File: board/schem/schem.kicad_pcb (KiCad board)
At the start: 2 copper layers, 133 x 85 mm, 136 parts, among them J1 no_break, J10 no_hal, J11 break2, J12 impulse, J13 hal, J14 no_temp, J15 speed, J16 analog, J17 motor_tmp, J18 adc_red1, J19 adc_red2, J2 motor_out, J20 ON/OFF, J21 lamp, J3 test, J8 POWER_IN, J9 break1, Q1 BC817, Q2 BC807, Q3 BC817, Q4 BC817, Q5 BC807, Q6 BC817, Q7 BC817, Q8 BC807, Q9 BC817, SW1 SW_Push, SW2 SW_Push, T1 NTD5865NL, T2 FDD9507L, T3 NTD5865NL, T4 FDD9507L, T5 NTD5865NL, T6 FDD9507L, U1 CFPS-39-12M, U10 AP2138, U11 LD1117, U2 EP4CE6, U3 JTAG, U4 IFX27001TFV50, U5 LF33CDT, U6 IS25LQ, U7 MPC3008, U8 IFX27001TFV50, U9 IS25LQ

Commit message: some  progress in  board  development
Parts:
- added R37: 4.7k, Resistor_SMD:R_1206_3216Metric, F.Cu at (203.2, 55.7)
- R42: moved to B.Cu
- moved R43 23.5 mm to (179.8, 68.0), turned to 270 degrees
- moved R36 14.4 mm to (210.0, 63.2), turned to 180 degrees
- moved R42 13.7 mm to (198.8, 83.5)
- moved R35 12.6 mm to (203.4, 67.8), turned to 90 degrees
- moved C4 11.2 mm to (197.6, 55.8), turned to 180 degrees
- moved R34 5.30 mm to (210.1, 60.2), turned to 180 degrees
- moved R39 4.90 mm to (197.2, 67.9), turned to 270 degrees
- moved J2 2.38 mm to (159.0, 88.6)
- moved U6 1.88 mm to (201.3, 60.9), turned to 0 degrees
- moved F2 1.20 mm to (112.7, 86.7)
- moved C15 0.95 mm to (154.0, 130.9)
- moved SW2 0.35 mm to (197.7, 130.2)
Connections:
- J3 pad 3: /control/A4 -> /control/A3
- J3 pad 4: /control/A3 -> /control/A4
- R35 pad 1: /control/ASDO -> Net-(R35-Pad1)
- U2 pad 43: Net-(U2-Pad43) -> /DriveAndSens/A_p
- U2 pad 44: Net-(U2-Pad44) -> /DriveAndSens/A_n
- U2 pad 50: Net-(U2-Pad50) -> /DriveAndSens/B_p
- U2 pad 51: Net-(U2-Pad51) -> /DriveAndSens/B_n
- U2 pad 54: /DriveAndSens/A_p -> Net-(U2-Pad54)
- U2 pad 55: /DriveAndSens/A_n -> Net-(U2-Pad55)
- U2 pad 58: /DriveAndSens/B_p -> Net-(U2-Pad58)
- U2 pad 59: /DriveAndSens/B_n -> Net-(U2-Pad59)
- U2 pad 69: /control/D_break -> Net-(U2-Pad69)
- U2 pad 70: /control/D_tmp -> Net-(U2-Pad70)
- U2 pad 71: /control/D_diag -> Net-(U2-Pad71)
- U6 pad 1: /control/nCSO -> /control/nCEO
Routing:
- net GND: track 0.00 -> 789.8 mm, vias 0 -> 20
- net +3V3: track 0.00 -> 609.1 mm, vias 0 -> 16
- net +1V2: track 0.00 -> 222.0 mm, vias 0 -> 5
- net +36V: track 0.00 -> 202.1 mm, vias 0 -> 1
- net +5V: track 0.00 -> 161.8 mm, vias 0 -> 4
- net +2V5: track 0.00 -> 140.1 mm, vias 0 -> 4
- net /DriveAndSens/A_n: track 0.00 -> 122.7 mm, vias 0 -> 1
- net /DriveAndSens/C_out: track 0.00 -> 50.9 mm
- net /DriveAndSens/B_out: track 0.00 -> 49.0 mm
- net /DriveAndSens/A_p: track 0.00 -> 48.1 mm, vias 0 -> 1
- net /control/nCONFIG: track 0.00 -> 44.2 mm, vias 0 -> 2
- net /control/hal_A: track 0.00 -> 44.2 mm, vias 0 -> 1
- net /control/TCK: track 0.00 -> 42.6 mm, vias 0 -> 1
- net /DriveAndSens/A_out: track 0.00 -> 41.9 mm, vias 0 -> 1
- net /control/A2: track 0.00 -> 38.4 mm
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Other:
- board size 133 x 85 mm -> 133 x 86 mm
- net class Default: clearance 0.25 -> 0.2; trace_width 0.25 -> 0.2
- rule trace_clearance: 0.25 -> 0.2

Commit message: some  work  on pcb
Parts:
- J2: footprint Connector_Phoenix_MSTB:PhoenixContact_MSTBA_2,5_3-G-5,08_1x03_P5.08mm_Horizontal -> Connector_Phoenix_MSTB:PhoenixContact_MSTBVA_2,5_3-G-5,08_1x03_P5.08mm_Vertical
- J20, J8: footprint Connector_Phoenix_MSTB:PhoenixContact_MSTBA_2,5_2-G-5,08_1x02_P5.08mm_Horizontal -> Connector_Phoenix_MSTB:PhoenixContact_MSTBVA_2,5_2-G-5,08_1x02_P5.08mm_Vertical
- moved R8 8.44 mm to (129.3, 126.7)
- moved R40 2.92 mm to (190.2, 124.5)
- moved J20 2.60 mm to (107.7, 61.0)
- moved J8 2.55 mm to (107.7, 75.2)
- moved T2 2.23 mm to (145.8, 124.3)
- moved R7 1.16 mm to (141.8, 129.2)
- moved T4 0.60 mm to (134.9, 93.2)
- moved C13 0.21 mm to (191.4, 104.0)
- turned SW2 to 180 degrees
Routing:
- net /DriveAndSens/A_p: track 48.1 -> 179.6 mm
- net +36V: track 202.1 -> 328.5 mm, vias 1 -> 6
- net /DriveAndSens/B_p: track 8.85 -> 101.5 mm
- net /DriveAndSens/B_n: track 14.6 -> 102.8 mm
- net +3V3: track 609.1 -> 686.8 mm
- net /DriveAndSens/A_n: track 122.7 -> 193.5 mm
- net /DriveAndSens/A_out: track 41.9 -> 106.2 mm
- net +2V5: track 140.1 -> 185.8 mm, vias 4 -> 6
- net /DriveAndSens/C_p: track 13.2 -> 44.3 mm, vias 1 -> 3
- net /DriveAndSens/B_out: track 49.0 -> 70.7 mm
- net /DriveAndSens/C_n: track 26.4 -> 46.8 mm, vias 0 -> 3
- net GND: track 789.8 -> 807.9 mm, vias 20 -> 21
- net Net-(C18-Pad1): track 1.31 -> 18.9 mm
- net Net-(Q9-Pad3): track 16.3 -> 31.8 mm
- net Net-(F2-Pad1): track 20.3 -> 35.7 mm, vias 2 -> 0
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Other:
- net class energy: clearance 1 -> 0.2
- net class energy_mid: clearance 0.5 -> 0.2

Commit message: some  work  on  pcb
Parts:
- removed F3: 3A, Fuse:Fuse_2512_6332Metric
- added R49: 4.7k, Resistor_SMD:R_1206_3216Metric, F.Cu at (215.0, 70.6)
- added R50: 4.7k, Resistor_SMD:R_1206_3216Metric, F.Cu at (214.8, 73.8)
- added R51: 4.7k, Resistor_SMD:R_1206_3216Metric, F.Cu at (212.3, 58.8)
- added R52: 4.7k, Resistor_SMD:R_1206_3216Metric, F.Cu at (229.9, 67.8)
- added R53: 4.7k, Resistor_SMD:R_1206_3216Metric, F.Cu at (223.3, 74.9)
- added R54: 4.7k, Resistor_SMD:R_1206_3216Metric, F.Cu at (229.9, 70.6)
- added R55: 63.4k, Resistor_SMD:R_1206_3216Metric, F.Cu at (132.6, 110.0)
- added R56: 10.5k, Resistor_SMD:R_1206_3216Metric, F.Cu at (119.5, 108.1)
- added R57: 2k, Resistor_SMD:R_1206_3216Metric, F.Cu at (125.8, 105.2)
- added U12: 68u, Inductor_SMD:L_12x12mm_H4.5mm, F.Cu at (110.8, 91.5)
- C10: value 0.1u -> 0.01u
- C11: value 10u -> 220u
- C17: value 0.1u -> 220u; footprint Capacitor_SMD:C_1206_3216Metric -> Capacitor_THT:CP_Radial_D8.0mm_P3.50mm
- C18: value 10u -> 0.22u; footprint Capacitor_THT:CP_Radial_D8.0mm_P3.50mm -> Capacitor_SMD:C_1206_3216Metric
- C4, C5: moved to B.Cu
- U4: value IFX27001TFV50 -> IS25LQ; footprint Package_TO_SOT_SMD:TO-252-2 -> Package_SO:SOIC-8_3.9x4.9mm_P1.27mm
- U8: value IFX27001TFV50 -> A8498; footprint Package_TO_SOT_SMD:TO-252-2 -> Package_SO:SOIC-8_3.9x4.9mm_P1.27mm
- U9: value IS25LQ -> B350B; footprint Package_SO:SOIC-8_3.9x4.9mm_P1.27mm -> Diode_SMD:D_SMB
- moved U4 107.9 mm to (222.4, 70.0), turned to 0 degrees
- moved U9 101.6 mm to (125.6, 100.8), turned to 0 degrees
- moved C18 55.1 mm to (129.8, 116.7)
- moved C17 49.7 mm to (115.5, 103.7)
- moved U8 47.6 mm to (125.8, 110.4)
- moved C1 45.1 mm to (185.1, 67.9), turned to 180 degrees
- moved U1 38.8 mm to (185.1, 71.8), turned to 270 degrees
- moved C11 17.3 mm to (116.0, 113.5), turned to 180 degrees
- moved R34 12.2 mm to (198.2, 57.5), turned to 0 degrees
- moved C10 11.8 mm to (126.6, 116.8), turned to 90 degrees
- moved R43 9.68 mm to (188.8, 71.7), turned to 90 degrees
- moved C4 8.47 mm to (204.7, 60.3), turned to 270 degrees
- moved R39 7.38 mm to (198.3, 60.6), turned to 0 degrees
- moved F1 6.39 mm to (112.7, 66.5)
- moved C5 6.19 mm to (222.2, 70.1), turned to 270 degrees
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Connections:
- net /control/ch2 renamed Net-(U7-Pad6)
- net /control/ch3 renamed Net-(U7-Pad7)
- net /control/ch4 renamed Net-(U7-Pad8)
- C10 pad 2: GND -> Net-(C10-Pad2)
- C11 pad 1: +5V -> +36V
- C17 pad 1: +36V -> Net-(C17-Pad1)
- C18 pad 1: Net-(C18-Pad1) -> +36V
- D5 pad 1: Net-(D5-Pad1) -> /control/D_hal
- F2 pad 1: Net-(F2-Pad1) -> +5V
- F2 pad 2: +36V -> Net-(C17-Pad1)
- J21 pad 2: Net-(C18-Pad1) -> +5V
- R34 pad 1: +3V3 -> /control/DATA0
- R35 pad 2: Net-(R35-Pad2) -> /control/ASDO
- R39 pad 1: Net-(R39-Pad1) -> +3V3
- R39 pad 2: /control/DATA0 -> Net-(R39-Pad2)
- R41 pad 2: Net-(R41-Pad2) -> /control/nCE_1
- U1 pad 3: Net-(U1-Pad3) -> /control/CLKIN
- U2 pad 12: Net-(U2-Pad12) -> /control/SCK
- U2 pad 128: /control/nCE_1 -> /control/SO_1
- U2 pad 129: /control/SI_1 -> /control/SCK_1
- U2 pad 132: /control/SO_1 -> /control/nCE_1
- U2 pad 133: /control/SCK_1 -> /control/SI_1
- U2 pad 32: Net-(U2-Pad32) -> /control/hal_C
- U2 pad 60: /DriveAndSens/C_p -> Net-(U2-Pad60)
- U2 pad 64: /DriveAndSens/C_n -> Net-(U2-Pad64)
- U2 pad 67: Net-(U2-Pad67) -> /control/D_hal
- U2 pad 68: /control/D_hal -> /control/D_break
- U2 pad 69: Net-(U2-Pad69) -> /control/D_tmp
- U2 pad 70: Net-(U2-Pad70) -> /control/D_diag
- U2 pad 71: Net-(U2-Pad71) -> /DriveAndSens/C_p
- U2 pad 72: Net-(U2-Pad72) -> /DriveAndSens/C_n
- U4 pad 1: GND -> /control/nCE_1
- U4 pad 2: +5V -> Net-(R49-Pad2)
- U4 pad 3: Net-(F2-Pad1) -> Net-(R50-Pad2)
- U6 pad 2: Net-(R39-Pad1) -> Net-(R34-Pad2)
- U6 pad 3: Net-(R34-Pad2) -> Net-(R39-Pad2)
- U6 pad 5: Net-(R35-Pad2) -> Net-(R35-Pad1)
- U6 pad 7: Net-(R34-Pad2) -> Net-(R51-Pad1)
- U8 pad 1: GND -> Net-(C10-Pad2)
- U8 pad 2: Net-(C18-Pad1) -> GND
- U9 pad 1: /control/nCE_1 -> Net-(C17-Pad1)
- U9 pad 2: /control/SO_1 -> GND
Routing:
- net GND: track 807.9 -> 880.8 mm, vias 21 -> 24
- net /control/hal_C: track 0.00 -> 70.5 mm, vias 0 -> 1
- net /control/D_hal: track 0.00 -> 68.2 mm
- net /control/D_break: track 0.00 -> 63.2 mm
- net /control/D_tmp: track 0.00 -> 59.0 mm
- net /control/D_diag: track 0.00 -> 53.3 mm
- net Net-(C17-Pad1): track 0.00 -> 50.7 mm
- net Net-(F2-Pad1): track 35.7 -> 0.00 mm
- net /control/SCK: track 5.47 -> 40.8 mm
- net Net-(U12-Pad1): track 0.00 -> 29.5 mm
- net +36V: track 328.5 -> 300.8 mm
- net +3V3: track 686.8 -> 711.6 mm, vias 16 -> 18
- net Net-(R41-Pad2): track 22.2 -> 0.00 mm
- net Net-(C18-Pad1): track 18.9 -> 0.00 mm
- net /control/ASDO: track 0.00 -> 14.4 mm
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
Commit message: work  on  pcb
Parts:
- D1, D12, D13, D2, D3, D4: value D -> BYC10
- R16: value 10k -> 1k
- R17, R18, R19: value 10k -> 4.7k
- moved D4 46.0 mm to (150.2, 69.5), turned to 0 degrees
- moved D2 41.9 mm to (132.5, 111.2), turned to 0 degrees
- moved D3 23.8 mm to (149.4, 86.0), turned to 270 degrees
- moved D1 11.0 mm to (147.2, 104.5)
- moved D12 5.05 mm to (162.3, 105.0), turned to 180 degrees
- moved C10 2.02 mm to (125.8, 114.9), turned to 0 degrees
- moved D13 1.10 mm to (168.5, 124.1), turned to 180 degrees
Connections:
- C10 pad 1: +36V -> Net-(C10-Pad1)
- D1 pad 1: +36V -> (no net)
- D1 pad 2: /DriveAndSens/B_out -> +36V
- D1 pad 3: (no net) -> /DriveAndSens/A_out
- D12 pad 1: +36V -> (no net)
- D12 pad 2: /DriveAndSens/C_out -> +36V
- D12 pad 3: (no net) -> /DriveAndSens/C_out
- D13 pad 1: /DriveAndSens/C_out -> (no net)
- D13 pad 2: Net-(D13-Pad2) -> /DriveAndSens/C_out
- D13 pad 3: (no net) -> Net-(D13-Pad3)
- D2 pad 1: /DriveAndSens/B_out -> (no net)
- D2 pad 2: Net-(D2-Pad2) -> /DriveAndSens/A_out
- D2 pad 3: (no net) -> Net-(D2-Pad3)
- D3 pad 1: +36V -> (no net)
- D3 pad 2: /DriveAndSens/A_out -> +36V
- D3 pad 3: (no net) -> /DriveAndSens/B_out
- D4 pad 1: /DriveAndSens/A_out -> (no net)
- D4 pad 2: Net-(D4-Pad2) -> /DriveAndSens/B_out
- D4 pad 3: (no net) -> Net-(D4-Pad3)
- T1 pad 3: Net-(D4-Pad2) -> Net-(D2-Pad3)
- T3 pad 3: Net-(D2-Pad2) -> Net-(D4-Pad3)
- T5 pad 3: Net-(D13-Pad2) -> Net-(D13-Pad3)
- U12 pad 1: Net-(U12-Pad1) -> Net-(C10-Pad1)
- U2 pad 94: +3V3 -> +2V5
- U2 pad 96: +3V3 -> +2V5
- U8 pad 7: Net-(U12-Pad1) -> Net-(C10-Pad1)
- U9 pad 1: Net-(C17-Pad1) -> Net-(C10-Pad1)
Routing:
- net Net-(C10-Pad1): track 0.00 -> 33.4 mm
- net Net-(D2-Pad3): track 0.00 -> 30.3 mm
- net Net-(U12-Pad1): track 29.5 -> 0.00 mm
- net +2V5: track 185.8 -> 208.5 mm
- net Net-(D13-Pad2): track 13.4 -> 0.00 mm
- net Net-(D2-Pad2): track 13.0 -> 0.00 mm
- net /DriveAndSens/A_out: track 106.2 -> 94.0 mm
- net Net-(D4-Pad2): track 12.1 -> 0.00 mm
- net Net-(D4-Pad3): track 0.00 -> 10.9 mm
- net Net-(C17-Pad1): track 50.7 -> 40.5 mm
- net /DriveAndSens/B_out: track 70.7 -> 80.1 mm
- net /DriveAndSens/C_out: track 64.5 -> 70.9 mm
- net +3V3: track 711.6 -> 705.6 mm
- net Net-(D13-Pad3): track 0.00 -> 5.66 mm
- net +1V2: track 229.7 -> 233.5 mm
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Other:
- net class power_micro added: clearance 0.2, trace_width 0.4, via_dia 0.8, via_drill 0.4

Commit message: recent  changes
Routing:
- net +36V: track 302.0 -> 337.2 mm
- net +1V2: track 233.5 -> 245.8 mm
- added copper zone on B.Cu, net GND
- added copper zone on F.Cu, net GND
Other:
- board size 133 x 86 mm -> 133 x 87 mm
- net class energy_mid: trace_width 2 -> 3

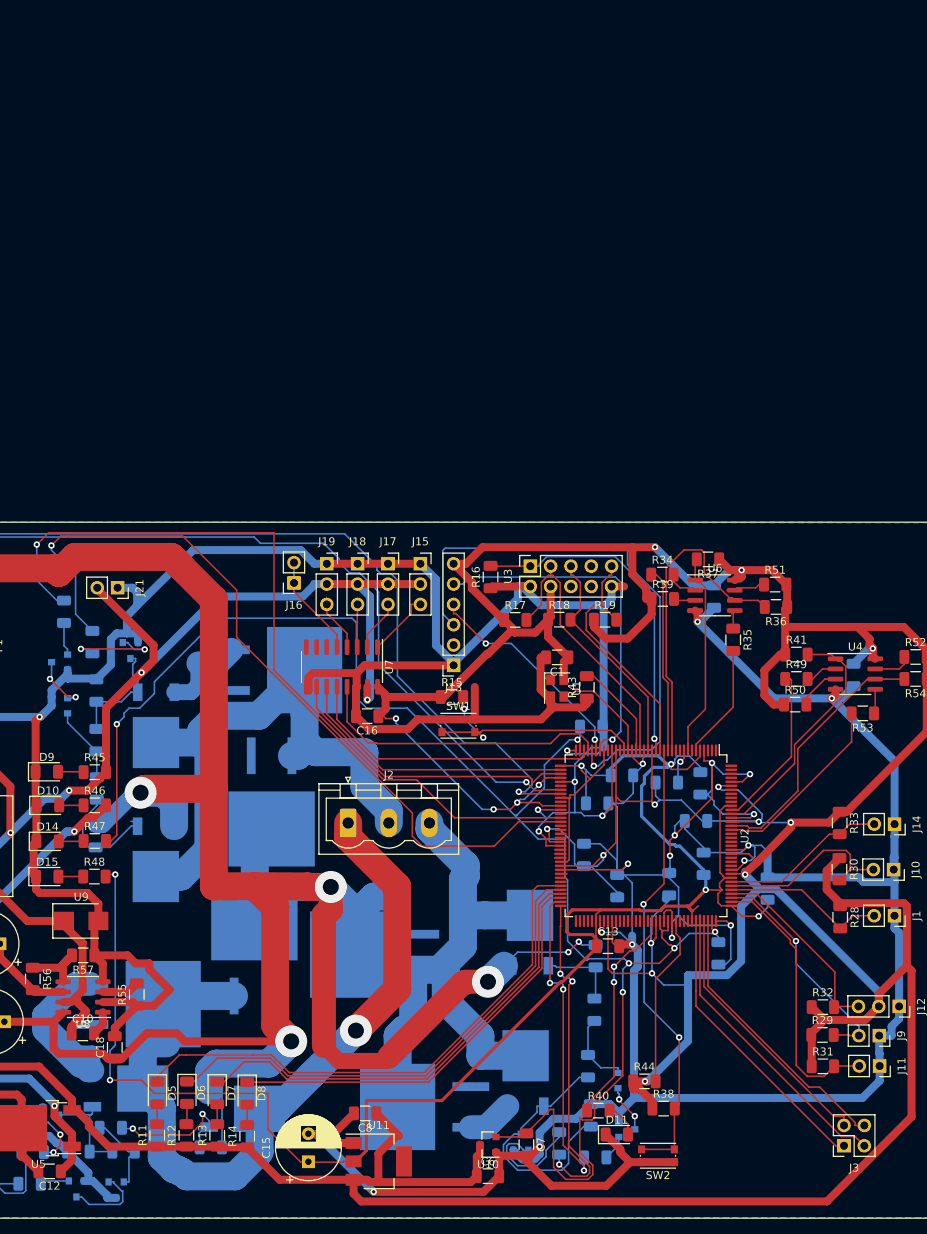
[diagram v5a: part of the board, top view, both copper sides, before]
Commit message: some  work  on schematic and  minor stuff in  adc  channel choice functionality
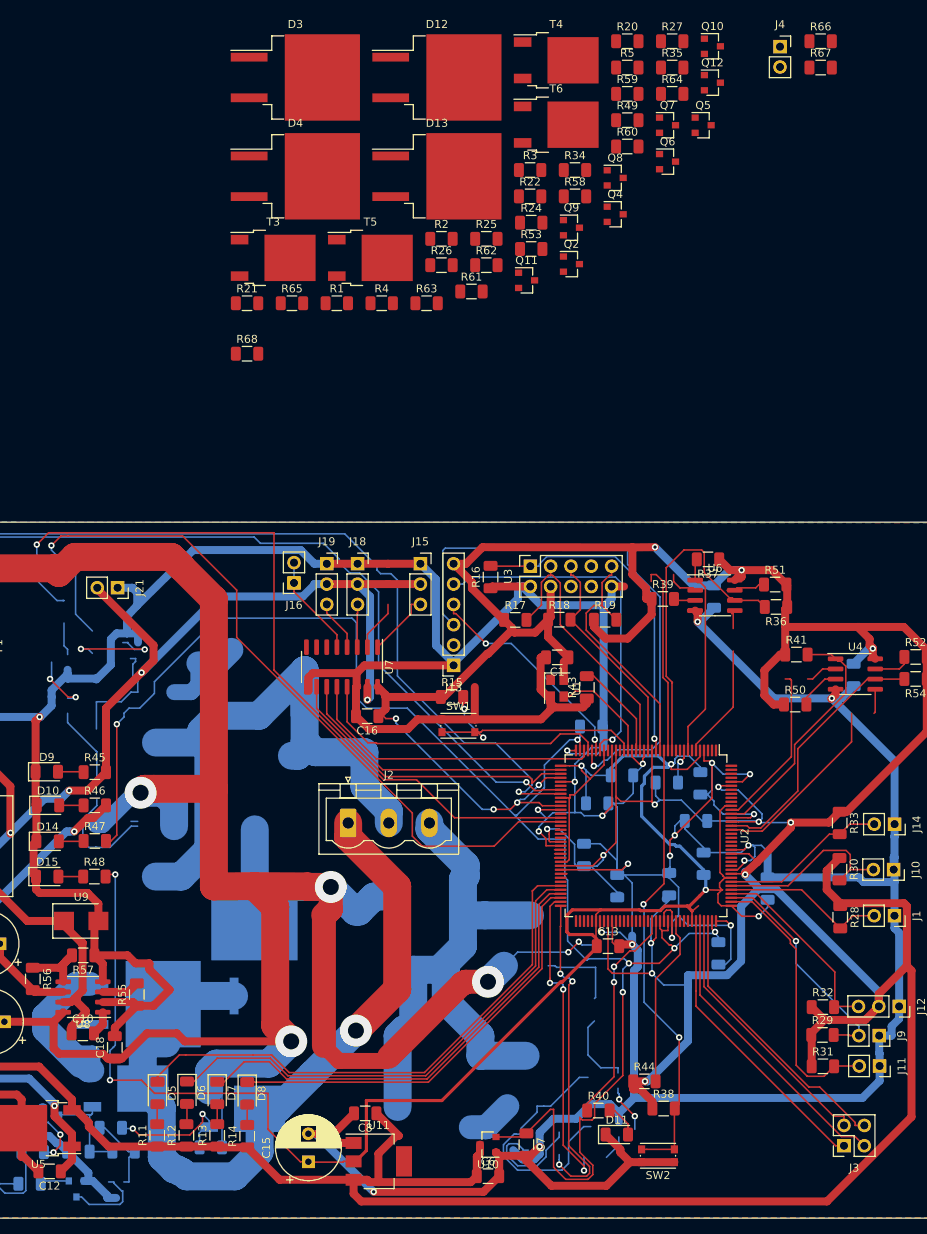
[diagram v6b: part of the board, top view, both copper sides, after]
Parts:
- removed J17: motor_tmp, Connector_PinSocket_2.54mm:PinSocket_1x03_P2.54mm_Vertical
- added J4: motor_tmp, Connector_PinSocket_2.54mm:PinSocket_1x02_P2.54mm_Vertical, F.Cu at (213.0, -8.43)
- added Q10: BC817, Package_TO_SOT_SMD:SOT-23, F.Cu at (204.5, -8.48)
- added Q11: BC817, Package_TO_SOT_SMD:SOT-23, F.Cu at (181.3, 20.8)
- added Q12: BC817, Package_TO_SOT_SMD:SOT-23, F.Cu at (204.5, -3.93)
- added R58: 8k, Resistor_SMD:R_1206_3216Metric, F.Cu at (187.3, 10.3)
- added R59: 100k, Resistor_SMD:R_1206_3216Metric, F.Cu at (193.9, -2.53)
- added R60: 10k, Resistor_SMD:R_1206_3216Metric, F.Cu at (193.9, 4.05)
- added R61: 4k, Resistor_SMD:R_1206_3216Metric, F.Cu at (174.4, 22.2)
- added R62: 10k, Resistor_SMD:R_1206_3216Metric, F.Cu at (176.2, 18.9)
- added R63: 10k, Resistor_SMD:R_1206_3216Metric, F.Cu at (168.8, 23.6)
- added R64: 10k, Resistor_SMD:R_1206_3216Metric, F.Cu at (199.5, -2.53)
- added R65: 10k, Resistor_SMD:R_1206_3216Metric, F.Cu at (151.9, 23.6)
- added R66: 4.7k, Resistor_SMD:R_1206_3216Metric, F.Cu at (218.0, -9.11)
- added R67: 4.7k, Resistor_SMD:R_1206_3216Metric, F.Cu at (218.0, -5.82)
- added R68: 120, Resistor_SMD:R_1206_3216Metric, F.Cu at (146.3, 29.9)
- D12, D13, D3, D4, Q4, Q6, Q7, Q9, R21, R22, T3, T4, T5, T6: moved to F.Cu
- Q2, Q5, Q8: value BC807 -> BC817; moved to F.Cu
- R1, R2: value 100k -> 2k; moved to F.Cu
- R10: value 7.5k -> 4k
- R20: value 7.5k -> 8k; moved to F.Cu
- R24: value 650 -> 10k; moved to F.Cu
- R25: value 2.2k -> 4k; moved to F.Cu
- R26: value 22k -> 2k; moved to F.Cu
- R27: value 7.5k -> 400k; moved to F.Cu
- R3: value 650 -> 400k; moved to F.Cu
- R34: value 4.7k -> 100k
- R35, R49: value 4.7k -> 10k
- R4: value 2.2k -> 100k; moved to F.Cu
- R5: value 22k -> 3k; moved to F.Cu
- R53: value 4.7k -> 3k
- R6: value 100k -> 400k
- R7: value 650 -> 3k
- R8: value 2.2k -> 8k
- R9: value 22k -> 10k
- moved R27 134.6 mm to (199.5, -9.11), turned to 0 degrees
- moved Q2 129.0 mm to (186.9, 18.7), turned to 0 degrees
- moved Q7 125.6 mm to (198.9, 1.39)
- moved R22 118.4 mm to (181.7, 10.3), turned to 0 degrees
- moved D13 116.3 mm to (170.1, 7.77), turned to 0 degrees
- moved R21 115.3 mm to (146.3, 23.6)
- moved Q9 114.5 mm to (186.9, 14.2), turned to 0 degrees
- moved Q8 112.8 mm to (192.4, 7.97)
- moved T4 111.8 mm to (185.0, -6.73), turned to 0 degrees
- moved D12 109.9 mm to (170.1, -4.58), turned to 0 degrees
- moved Q5 108.3 mm to (203.3, 1.39), turned to 0 degrees
- moved R5 107.1 mm to (193.9, -5.82), turned to 0 degrees
- moved R20 104.8 mm to (193.9, -9.11), turned to 0 degrees
- moved T5 103.7 mm to (161.8, 18.0), turned to 0 degrees
- moved R26 101.8 mm to (170.6, 18.9), turned to 0 degrees
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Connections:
- D11 pad 1: GND -> Net-(D11-Pad1)
- D11 pad 2: Net-(D11-Pad2) -> +3V3
- D13 pad 3: Net-(D13-Pad3) -> GND
- D2 pad 3: Net-(D2-Pad3) -> GND
- D4 pad 3: Net-(D4-Pad3) -> GND
- Q2 pad 1: Net-(Q1-Pad3) -> Net-(Q2-Pad1)
- Q2 pad 2: Net-(Q2-Pad2) -> GND
- Q2 pad 3: GND -> Net-(Q2-Pad3)
- Q4 pad 3: Net-(Q4-Pad3) -> Net-(Q3-Pad1)
- Q5 pad 1: Net-(Q4-Pad3) -> Net-(Q5-Pad1)
- Q5 pad 2: Net-(Q5-Pad2) -> GND
- Q5 pad 3: GND -> Net-(Q5-Pad3)
- Q6 pad 1: Net-(Q6-Pad1) -> Net-(Q5-Pad3)
- Q8 pad 1: Net-(Q7-Pad3) -> Net-(Q8-Pad1)
- Q8 pad 2: Net-(Q8-Pad2) -> GND
- Q8 pad 3: GND -> Net-(Q10-Pad1)
- Q9 pad 2: GND -> /DriveAndSens/adc_A
- Q9 pad 3: Net-(Q9-Pad3) -> +3V3
- R1 pad 1: /DriveAndSens/B_p -> /DriveAndSens/A_p
- R1 pad 2: Net-(Q4-Pad1) -> Net-(Q1-Pad1)
- R2 pad 1: /DriveAndSens/B_n -> /DriveAndSens/B_p
- R2 pad 2: Net-(Q6-Pad1) -> Net-(Q2-Pad1)
- R20 pad 1: Net-(Q6-Pad3) -> Net-(R20-Pad1)
- R20 pad 2: GND -> Net-(Q2-Pad3)
- R21 pad 1: /DriveAndSens/C_p -> +36V
- R21 pad 2: Net-(Q7-Pad1) -> Net-(Q3-Pad1)
- R22 pad 1: /DriveAndSens/C_n -> +36V
- R22 pad 2: Net-(Q9-Pad1) -> Net-(Q5-Pad3)
- R23 pad 2: Net-(Q3-Pad1) -> Net-(Q4-Pad1)
- R24 pad 2: Net-(R24-Pad2) -> Net-(Q6-Pad3)
- R25 pad 1: Net-(R24-Pad2) -> Net-(Q6-Pad3)
- R25 pad 2: Net-(Q8-Pad2) -> GND
- R26 pad 1: Net-(Q8-Pad2) -> /DriveAndSens/C_p
- R26 pad 2: Net-(Q9-Pad3) -> Net-(Q7-Pad1)
- R27 pad 1: Net-(Q9-Pad3) -> Net-(Q7-Pad1)
- R27 pad 2: GND -> +36V
- R3 pad 1: +36V -> Net-(Q2-Pad1)
- R3 pad 2: Net-(R3-Pad2) -> +36V
- R34 pad 1: /control/DATA0 -> /DriveAndSens/C_n
- R34 pad 2: Net-(R34-Pad2) -> Net-(Q8-Pad1)
- R35 pad 1: Net-(R35-Pad1) -> /DriveAndSens/A_out
- R35 pad 2: /control/ASDO -> Net-(Q9-Pad1)
- R4 pad 1: Net-(R3-Pad2) -> /DriveAndSens/B_n
- R4 pad 2: Net-(Q5-Pad2) -> Net-(Q5-Pad1)
- R40 pad 2: Net-(D11-Pad2) -> Net-(D11-Pad1)
- R49 pad 1: /control/SI_1 -> Net-(Q9-Pad1)
- R49 pad 2: Net-(R49-Pad2) -> GND
- R5 pad 1: Net-(Q5-Pad2) -> +36V
- R5 pad 2: Net-(Q6-Pad3) -> Net-(R20-Pad1)
- R53 pad 1: Net-(R53-Pad1) -> +36V
- R53 pad 2: /control/SO_1 -> Net-(R53-Pad2)
- R6 pad 1: /DriveAndSens/A_p -> Net-(Q1-Pad1)
- R6 pad 2: Net-(Q1-Pad1) -> +36V
- R8 pad 2: Net-(Q2-Pad2) -> Net-(Q1-Pad3)
- R9 pad 1: Net-(Q2-Pad2) -> +36V
- T1 pad 3: Net-(D2-Pad3) -> GND
- T3 pad 3: Net-(D4-Pad3) -> GND
- T4 pad 1: Net-(R3-Pad2) -> Net-(R20-Pad1)
- T5 pad 1: Net-(Q9-Pad3) -> Net-(Q10-Pad3)
- T5 pad 3: Net-(D13-Pad3) -> GND
- T6 pad 1: Net-(R24-Pad2) -> Net-(R53-Pad2)
- U4 pad 2: Net-(R49-Pad2) -> /control/SI_1
- U4 pad 5: Net-(R53-Pad1) -> /control/SO_1
- U6 pad 2: Net-(R34-Pad2) -> /control/DATA0
- U6 pad 5: Net-(R35-Pad1) -> /control/ASDO
- U7 pad 6: Net-(U7-Pad6) -> /DriveAndSens/adc_A
- U7 pad 7: Net-(U7-Pad7) -> /DriveAndSens/adc_B
- U7 pad 8: Net-(U7-Pad8) -> /DriveAndSens/adc_C
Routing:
- net GND: track 878.7 -> 909.0 mm
- net Net-(D2-Pad3): track 30.3 -> 0.00 mm
- net Net-(R34-Pad2): track 4.38 -> 0.00 mm
- net /control/DATA0: track 24.1 -> 28.5 mm
- net Net-(R49-Pad2): track 4.02 -> 0.00 mm
- net /control/SI_1: track 21.6 -> 25.6 mm
- net Net-(R53-Pad1): track 3.07 -> 0.00 mm
- net /control/SO_1: track 23.3 -> 26.4 mm
- net /control/ASDO: track 14.4 -> 17.3 mm
- net Net-(R35-Pad1): track 2.90 -> 0.00 mm
